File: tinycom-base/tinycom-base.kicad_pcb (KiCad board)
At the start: 2 copper layers, 45.2 x 45.2 mm, 38 parts, among them J1 MICRO_SD_HINGE, P1 CONN_02X08, P2 CONN_02X08, P3 USB_A, P4 USB_B, U1 SY8008BAAC, U2 SY8008BAAC, U3 SY8008BAAC

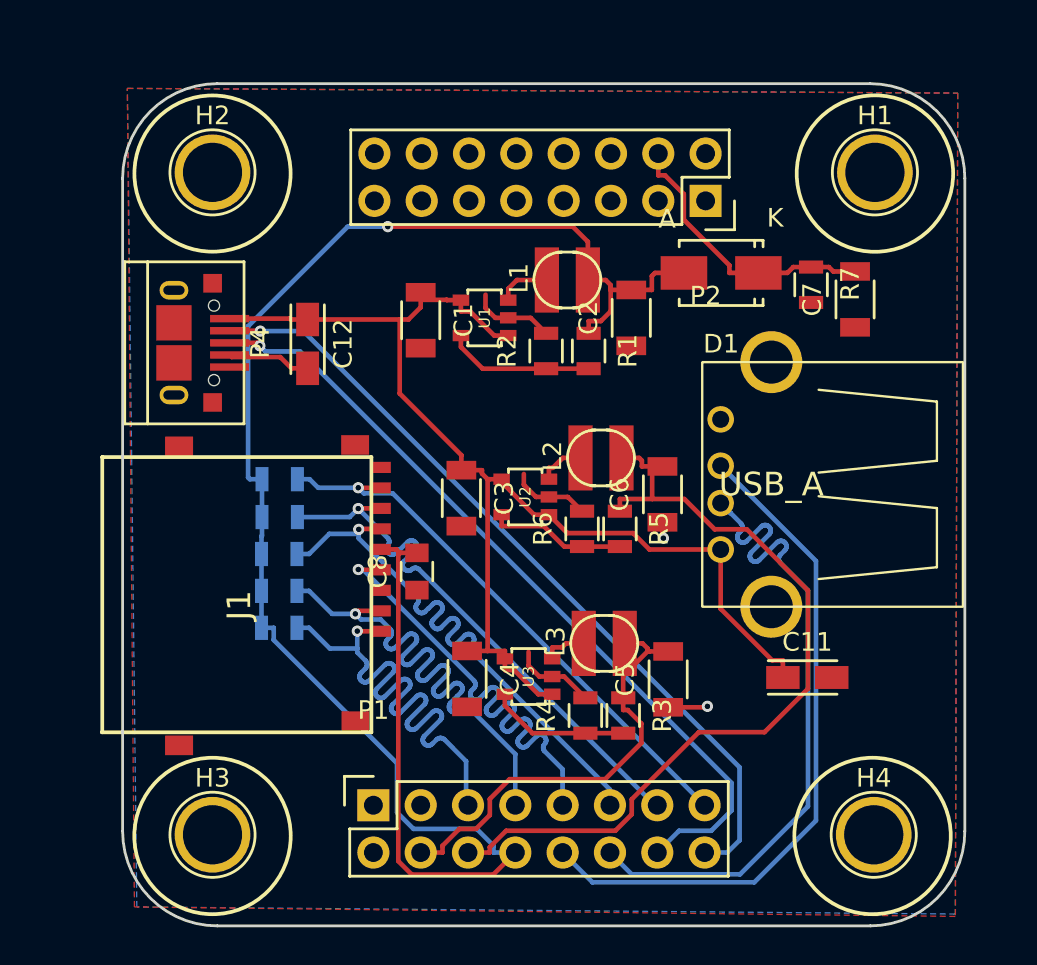
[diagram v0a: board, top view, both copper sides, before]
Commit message: add uboot_sel test point
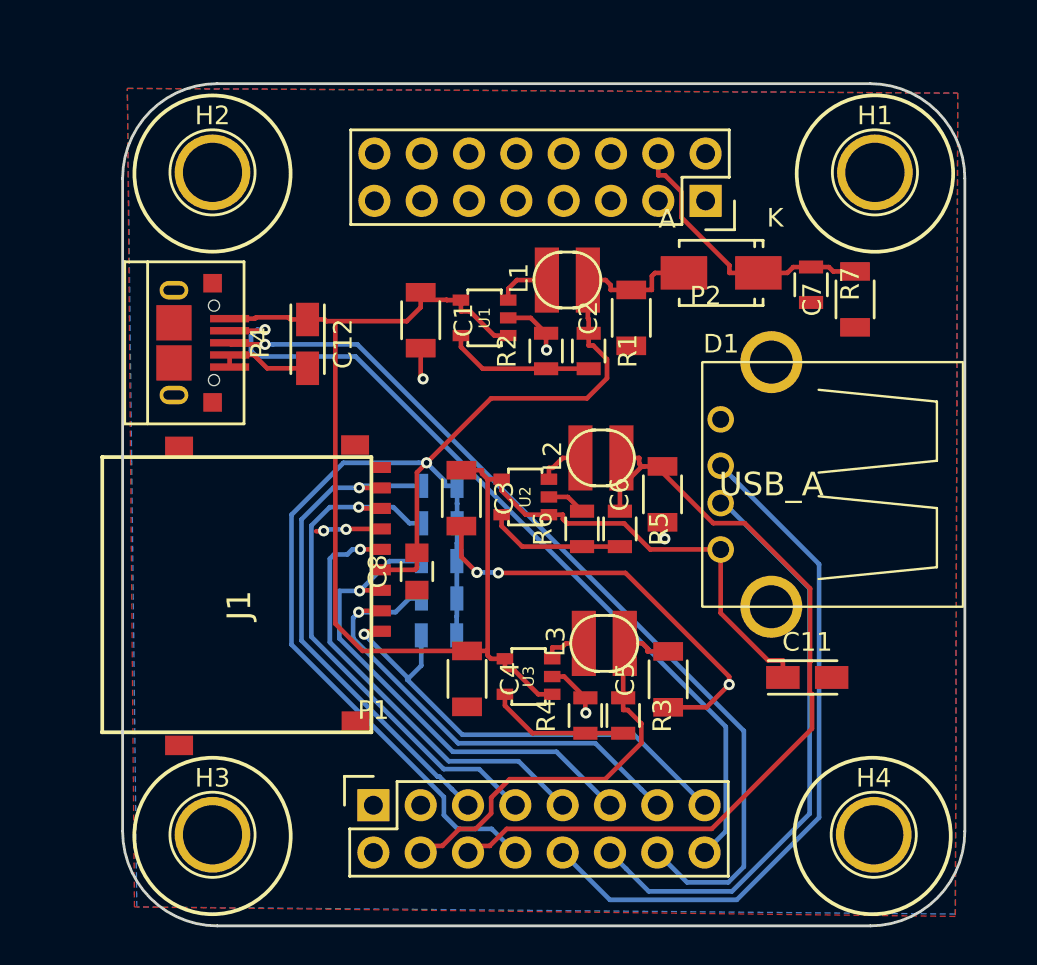
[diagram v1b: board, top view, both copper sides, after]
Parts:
- P4: value USB_B -> USB_OTG
- moved R12 12.0 mm to (141.4, 108.9), turned to 180 degrees
- moved R8 11.5 mm to (141.5, 100.8), turned to 180 degrees
- moved R11 9.61 mm to (141.5, 106.9), turned to 180 degrees
- moved R9 9.34 mm to (141.5, 102.8), turned to 180 degrees
- moved R10 8.59 mm to (141.5, 104.9), turned to 180 degrees
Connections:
- P4 pad 5: (no net) -> GND
- P4 pad 6: (no net) -> GND
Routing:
- net GND: track 20.8 -> 42.7 mm, vias 2 -> 9
- net VCC_33: track 95.8 -> 74.5 mm
- net +5V: track 66.6 -> 81.5 mm
- net UDP0: track 43.1 -> 49.2 mm
- net UDM1: track 37.6 -> 32.6 mm
- net SDC0_D2: track 30.3 -> 25.8 mm
- net SDC0_D3: track 30.3 -> 26.5 mm
- net SDC0_CMD: track 30.6 -> 27.0 mm
- net SDC0_CLK: track 26.7 -> 23.6 mm
- net SDC0_D1: track 30.5 -> 27.5 mm
- net SDC0_D0: track 30.5 -> 28.6 mm
- net UDM0: track 43.2 -> 44.7 mm
- net UDP1: track 36.8 -> 37.7 mm

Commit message: xxx
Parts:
- C12: footprint Capacitors_Tantalum_SMD:TantalC_SizeA_EIA-3216_Reflow -> Capacitors_Tantalum_SMD:TantalC_SizeB_EIA-3528_Reflow
- moved C12 0.12 mm to (134.3, 93.2)
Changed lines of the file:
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@@
     (links 90)
     (no_connects 0)
-    (area 124.384999 79.172999 169.747001 124.535001)
+    (area 122.516 73.697334 169.783501 124.987666)
     (thickness 1.6)
     (drawings 14)
@@
   )
   (module Capacitors_Tantalum_SMD:TantalC_SizeA_EIA-3216_Reflow (layer F.Cu)
-    (at 134.391 93.218 270)
-    (descr "Tantal Cap. , Size A, EIA-3216, Reflow")
-    (tags "Tantal Capacitor Size-A EIA-3216 reflow")
-    (attr smd)
-    (fp_text reference C12 (at 0 -1.9 270) (layer F.SilkS)
-      (effects (font (size 1 1) (thickness 0.15)))
-    )
-    (fp_text value CP_Small (at 0 2.1 270) (layer F.Fab)
-      (effects (font (size 1 1) (thickness 0.15)))
-    )
-    (fp_line (start 1.6 0.9) (end -2.1 0.9) (layer F.SilkS) (width 0.15))
-    (fp_line (start 1.6 -0.9) (end -2.1 -0.9) (layer F.SilkS) (width 0.15))
-    (fp_line (start -2.5 1.2) (end 2.5 1.2) (layer F.CrtYd) (width 0.05))
-    (fp_line (start 2.5 1.2) (end 2.5 -1.2) (layer F.CrtYd) (width 0.05))
-    (fp_line (start 2.5 -1.2) (end -2.5 -1.2) (layer F.CrtYd) (width 0.05))
-    (fp_line (start -2.5 -1.2) (end -2.5 1.2) (layer F.CrtYd) (width 0.05))
-    (pad 2 smd rect (at 1.31 0 270) (size 1.8 1.23) (layers F.Cu F.Paste F.Mask)
-      (net 2 GND))
-    (pad 1 smd rect (at -1.31 0 270) (size 1.8 1.23) (layers F.Cu F.Paste F.Mask)
-      (net 1 +5V))
-    (model Capacitors_Tantalum_SMD.3dshapes/TantalC_SizeA_EIA-3216_Reflow.wrl
-      (at (xyz 0 0 0))
-      (scale (xyz 1 1 1))
-      (rotate (xyz 0 0 180))
-    )
-  )
-  (module Capacitors_Tantalum_SMD:TantalC_SizeA_EIA-3216_Reflow (layer F.Cu)
     (at 161.214 111.125)
     (descr "Tantal Cap. , Size A, EIA-3216, Reflow")
@@
     (pad 6 smd rect (at 3.2 -0.9) (size 1 1) (layers F.Cu F.Paste F.Mask)
       (net 2 GND))
+  )
+  (module Capacitors_Tantalum_SMD:TantalC_SizeB_EIA-3528_Reflow (layer F.Cu)
+    (at 134.27202 93.19972 270)
+    (descr "Tantal Cap. , Size B, EIA-3528, Reflow")
+    (tags "Tantal Capacitor Size-B EIA-3528 Reflow")
+    (attr smd)
+    (fp_text reference C12 (at 0 -2.6 270) (layer F.SilkS)
+      (effects (font (size 1 1) (thickness 0.15)))
+    )
+    (fp_text value CP_Small (at 0 2.7 270) (layer F.Fab)
+      (effects (font (size 1 1) (thickness 0.15)))
+    )
+    (fp_line (start 2.7 -1.8) (end -2.7 -1.8) (layer F.CrtYd) (width 0.05))
+    (fp_line (start -2.7 -1.8) (end -2.7 1.8) (layer F.CrtYd) (width 0.05))
+    (fp_line (start -2.7 1.8) (end 2.7 1.8) (layer F.CrtYd) (width 0.05))
+    (fp_line (start 2.7 1.8) (end 2.7 -1.8) (layer F.CrtYd) (width 0.05))
+    (fp_line (start 1.8 1.5) (end -2.3 1.5) (layer F.SilkS) (width 0.15))
+    (fp_line (start 1.8 -1.5) (end -2.3 -1.5) (layer F.SilkS) (width 0.15))
+    (pad 2 smd rect (at 1.46 0 270) (size 1.8 2.23) (layers F.Cu F.Paste F.Mask)
+      (net 2 GND))
+    (pad 1 smd rect (at -1.46 0 270) (size 1.8 2.23) (layers F.Cu F.Paste F.Mask)
+      (net 1 +5V))
+    (model Capacitors_Tantalum_SMD.3dshapes/TantalC_SizeB_EIA-3528_Reflow.wrl
+      (at (xyz 0 0 0))
+      (scale (xyz 1 1 1))
+      (rotate (xyz 0 0 180))
+    )
   )
   (gr_text http://tinycom.org/ (at 146.939 104.648) (layer B.SilkS)
@@
   (segment (start 144.0551 100.4825) (end 144.0551 109.701) (width 0.25) (layer F.Cu) (net 1))
   (segment (start 144.805 100.4825) (end 144.805 101.0926) (width 0.25) (layer F.Cu) (net 1))
+  (via (at 153.5684 103.67949) (size 0.6) (drill 0.3) (layers F.Cu B.Cu) (net 2))
   (segment (start 130.20354 93.812) (end 130.20354 94.462) (width 0.25) (layer F.Cu) (net 2))
   (segment (start 135.2296 103.2764) (end 134.8486 103.2764) (width 0.25) (layer F.Cu) (net 2))
@@
   (segment (start 153.441 102.795) (end 153.441 103.55209) (width 0.25) (layer F.Cu) (net 2))
   (segment (start 153.441 103.55209) (end 153.5684 103.67949) (width 0.25) (layer F.Cu) (net 2))
-  (via (at 153.5684 103.67949) (size 0.6) (drill 0.3) (layers F.Cu B.Cu) (net 2))
   (segment (start 140.462 93.448) (end 140.462 94.9706) (width 0.25) (layer F.Cu) (net 2))
   (segment (start 140.462 94.9706) (end 140.589 95.0976) (width 0.25) (layer F.Cu) (net 2))

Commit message: rename wifi->basse
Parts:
- removed C8: C_Small, Capacitors_SMD:C_0805
- removed R10, R11, R12, R8, R9: R_Small, Resistors_SMD:R_0805
- added HDMI1: HDMI-SWM-19, tinycom:HDMI-SWM-19, F.Cu at (128.6, 107.3)
- added U4: RTL8723BS(ComboModule), tinycom:RL-SM02BD(RTL8723BS), F.Cu at (146.8, 108.1)
- J1: moved to B.Cu
- moved J1 44.2 mm to (168.4, 102.1)
- moved C12 36.4 mm to (165.9, 111.2), turned to 0 degrees
- moved C11 35.4 mm to (132.2, 90.8), turned to 90 degrees
- moved C5 22.1 mm to (153.6, 89.1), turned to 180 degrees
- moved R3 22.1 mm to (155.6, 91.5), turned to 0 degrees
- moved R4 20.6 mm to (155.6, 93.5), turned to 180 degrees
- moved C4 18.9 mm to (155.5, 97.1)
- moved L3 16.8 mm to (151.7, 92.5), turned to 180 degrees
- moved U3 15.6 mm to (152.1, 96.6), turned to 180 degrees
- moved C6 14.2 mm to (146.0, 89.2), turned to 180 degrees
- moved C2 13.9 mm to (138.1, 89.1), turned to 180 degrees
- moved L1 12.6 mm to (136.1, 92.5), turned to 180 degrees
- moved R5 12.1 mm to (147.9, 91.5), turned to 0 degrees
- moved R1 9.84 mm to (139.9, 91.4), turned to 0 degrees
- moved R6 9.70 mm to (147.9, 93.5), turned to 180 degrees
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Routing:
- net +5V: track 81.5 -> 0.00 mm
- net VCC_33: track 74.5 -> 0.00 mm, vias 1 -> 0
- net UDP0: track 49.2 -> 0.00 mm, vias 1 -> 0
- net VCC_14: track 45.3 -> 0.00 mm
- net UDM0: track 44.7 -> 0.00 mm, vias 1 -> 0
- net GND: track 42.7 -> 0.00 mm, vias 9 -> 0
- net UDP1: track 37.7 -> 0.00 mm
- net UDM1: track 32.6 -> 0.00 mm
- net SDC0_D0: track 28.6 -> 0.00 mm, vias 1 -> 0
- net SDC0_D1: track 27.5 -> 0.00 mm, vias 1 -> 0
- net SDC0_CMD: track 27.0 -> 0.00 mm, vias 1 -> 0
- net SDC0_D3: track 26.5 -> 0.00 mm, vias 1 -> 0
- net SDC0_D2: track 25.8 -> 0.00 mm, vias 1 -> 0
- net SDC0_CLK: track 23.6 -> 0.00 mm, vias 1 -> 0
- net VCC_15: track 23.4 -> 0.00 mm
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
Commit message: improve base board
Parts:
- added C8: C_Small, Capacitors_SMD:C_0805, B.Cu at (157.4, 99.8)
- added U5: rainsun-antenna, tinycom:rainsun-antenna, F.Cu at (158.8, 112.7)
- added U6: sata-smd, Connect:SATA-7_SMD, B.Cu at (170.9, 102.0)
- P1, P2: value CONN_02X08 -> CONN_02X10; footprint Socket_Strips:Socket_Strip_Straight_2x08 -> Socket_Strips:Socket_Strip_Straight_2x10
- U4: value RTL8723BS(ComboModule) -> RTL8188; footprint tinycom:RL-SM02BD(RTL8723BS) -> tinycom:RTL8188
- moved J1 42.7 mm to (125.8, 101.3), turned to 270 degrees
- moved P2 20.3 mm to (135.6, 82.9), turned to 0 degrees
- moved C12 11.8 mm to (155.1, 106.5), turned to 270 degrees
- moved P1 2.32 mm to (135.6, 118.2)
- moved P4 1.02 mm to (127.0, 92.7)
- moved U4 0.98 mm to (146.3, 109.0), turned to 180 degrees
- moved HDMI1 0.94 mm to (129.2, 108.1)
- moved C4 0.64 mm to (155.0, 96.7)
- moved C3 0.60 mm to (147.3, 96.8)
- moved C1 0.49 mm to (139.4, 97.0)
- moved C2 0.17 mm to (138.0, 89.0)
- moved C5 0.17 mm to (153.5, 89.0)
- moved L2 0.17 mm to (143.9, 92.4)
- moved L3 0.17 mm to (151.6, 92.4)
- moved R3 0.17 mm to (155.4, 91.4)
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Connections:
- HDMI1 pad 1: (no net) -> HTX2P
- HDMI1 pad 10: (no net) -> HTXCP
- HDMI1 pad 11: (no net) -> GND
- HDMI1 pad 12: (no net) -> HTXCN
- HDMI1 pad 13: (no net) -> HCEC
- HDMI1 pad 15: (no net) -> HCSL
- HDMI1 pad 16: (no net) -> HSDA
- HDMI1 pad 17: (no net) -> GND
- HDMI1 pad 18: (no net) -> +5V
- HDMI1 pad 19: (no net) -> HHPD
- HDMI1 pad 2: (no net) -> GND
- HDMI1 pad 3: (no net) -> HTX2N
- HDMI1 pad 4: (no net) -> HTX1P
- HDMI1 pad 5: (no net) -> GND
- HDMI1 pad 6: (no net) -> HTX1N
- HDMI1 pad 7: (no net) -> HTX0P
- HDMI1 pad 8: (no net) -> GND
- HDMI1 pad 9: (no net) -> HTX0N
- P1 pad 1: (no net) -> HTX2P
- P1 pad 11: SDC0_CMD -> HTX0N
- P1 pad 13: SDC0_D3 -> HTXCP
- P1 pad 14: UDP0 -> UDP2
- P1 pad 15: SDC0_D2 -> HTXCN
- P1 pad 16: UDM0 -> UDM2
- P1 pad 3: (no net) -> HTX2N
- P1 pad 4: VCC_15 -> GND
- P1 pad 5: SDC0_D1 -> HTX1P
- P1 pad 6: VCC_14 -> UDP0
- P1 pad 7: SDC0_D0 -> HTX1N
- P1 pad 8: VCC_33 -> UDM0
- P1 pad 9: SDC0_CLK -> HTX0P
- P2 pad 1: (no net) -> VCC_33
- P2 pad 10: (no net) -> SDC0_D2
- P2 pad 12: (no net) -> SDC0_D3
- P2 pad 14: (no net) -> SDC0_CMD
- P2 pad 16: (no net) -> SDC0_CLK
- P2 pad 2: GND -> (no net)
- P2 pad 3: (no net) -> VCC_30
- P2 pad 4: VCC_30 -> (no net)
- P2 pad 7: (no net) -> VCC_15
- P2 pad 9: (no net) -> VCC_14
- U4 pad 1: (no net) -> GND
- U4 pad 2: (no net) -> UDP2
- U4 pad 3: (no net) -> UDM2
- U4 pad 4: (no net) -> VCC_33
- U4 pad 5: (no net) -> GND
- U4 pad 6: (no net) -> Net-(U4-Pad6)
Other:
- net class Default: clearance 0.15 -> 0.2; trace_width 0.25 -> 0.2
- rule trace_clearance: 0.15 -> 0.2

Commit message: move sata
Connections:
- P2 pad 10: SDC0_D2 -> SDC0_D0
- P2 pad 12: SDC0_D3 -> SDC0_D1
- P2 pad 14: SDC0_CMD -> (no net)
- P2 pad 16: SDC0_CLK -> (no net)
- P2 pad 18: SDC0_D0 -> (no net)
- P2 pad 2: (no net) -> SDC0_D2
- P2 pad 20: SDC0_D1 -> (no net)
- P2 pad 4: (no net) -> SDC0_D3
- P2 pad 6: (no net) -> SDC0_CMD
- P2 pad 8: (no net) -> SDC0_CLK
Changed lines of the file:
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@@
   (general
     (links 106)
-    (no_connects 82)
+    (no_connects 83)
     (area 124.384999 79.172999 169.747001 124.535001)
     (thickness 1.6)
@@
     (pad 1 thru_hole rect (at 0 0) (size 1.7272 1.7272) (drill 1.016) (layers *.Cu *.Mask F.SilkS)
       (net 5 VCC_33))
-    (pad 2 thru_hole oval (at 0 2.54) (size 1.7272 1.7272) (drill 1.016) (layers *.Cu *.Mask F.SilkS))
+    (pad 2 thru_hole oval (at 0 2.54) (size 1.7272 1.7272) (drill 1.016) (layers *.Cu *.Mask F.SilkS)
+      (net 33 SDC0_D2))
     (pad 3 thru_hole oval (at 2.54 0) (size 1.7272 1.7272) (drill 1.016) (layers *.Cu *.Mask F.SilkS)
       (net 9 VCC_30))
-    (pad 4 thru_hole oval (at 2.54 2.54) (size 1.7272 1.7272) (drill 1.016) (layers *.Cu *.Mask F.SilkS))
+    (pad 4 thru_hole oval (at 2.54 2.54) (size 1.7272 1.7272) (drill 1.016) (layers *.Cu *.Mask F.SilkS)
+      (net 32 SDC0_D3))
     (pad 5 thru_hole oval (at 5.08 0) (size 1.7272 1.7272) (drill 1.016) (layers *.Cu *.Mask F.SilkS))
-    (pad 6 thru_hole oval (at 5.08 2.54) (size 1.7272 1.7272) (drill 1.016) (layers *.Cu *.Mask F.SilkS))
+    (pad 6 thru_hole oval (at 5.08 2.54) (size 1.7272 1.7272) (drill 1.016) (layers *.Cu *.Mask F.SilkS)
+      (net 31 SDC0_CMD))
     (pad 7 thru_hole oval (at 7.62 0) (size 1.7272 1.7272) (drill 1.016) (layers *.Cu *.Mask F.SilkS)
       (net 3 VCC_15))
-    (pad 8 thru_hole oval (at 7.62 2.54) (size 1.7272 1.7272) (drill 1.016) (layers *.Cu *.Mask F.SilkS))
+    (pad 8 thru_hole oval (at 7.62 2.54) (size 1.7272 1.7272) (drill 1.016) (layers *.Cu *.Mask F.SilkS)
+      (net 30 SDC0_CLK))
     (pad 9 thru_hole oval (at 10.16 0) (size 1.7272 1.7272) (drill 1.016) (layers *.Cu *.Mask F.SilkS)
       (net 4 VCC_14))
     (pad 10 thru_hole oval (at 10.16 2.54) (size 1.7272 1.7272) (drill 1.016) (layers *.Cu *.Mask F.SilkS)
-      (net 33 SDC0_D2))
+      (net 29 SDC0_D0))
     (pad 11 thru_hole oval (at 12.7 0) (size 1.7272 1.7272) (drill 1.016) (layers *.Cu *.Mask F.SilkS))
     (pad 12 thru_hole oval (at 12.7 2.54) (size 1.7272 1.7272) (drill 1.016) (layers *.Cu *.Mask F.SilkS)
-      (net 32 SDC0_D3))
+      (net 28 SDC0_D1))
     (pad 13 thru_hole oval (at 15.24 0) (size 1.7272 1.7272) (drill 1.016) (layers *.Cu *.Mask F.SilkS))
-    (pad 14 thru_hole oval (at 15.24 2.54) (size 1.7272 1.7272) (drill 1.016) (layers *.Cu *.Mask F.SilkS)
-      (net 31 SDC0_CMD))
+    (pad 14 thru_hole oval (at 15.24 2.54) (size 1.7272 1.7272) (drill 1.016) (layers *.Cu *.Mask F.SilkS))
     (pad 15 thru_hole oval (at 17.78 0) (size 1.7272 1.7272) (drill 1.016) (layers *.Cu *.Mask F.SilkS))
-    (pad 16 thru_hole oval (at 17.78 2.54) (size 1.7272 1.7272) (drill 1.016) (layers *.Cu *.Mask F.SilkS)
-      (net 30 SDC0_CLK))
+    (pad 16 thru_hole oval (at 17.78 2.54) (size 1.7272 1.7272) (drill 1.016) (layers *.Cu *.Mask F.SilkS))
     (pad 17 thru_hole oval (at 20.32 0) (size 1.7272 1.7272) (drill 1.016) (layers *.Cu *.Mask F.SilkS))
-    (pad 18 thru_hole oval (at 20.32 2.54) (size 1.7272 1.7272) (drill 1.016) (layers *.Cu *.Mask F.SilkS)
-      (net 29 SDC0_D0))
+    (pad 18 thru_hole oval (at 20.32 2.54) (size 1.7272 1.7272) (drill 1.016) (layers *.Cu *.Mask F.SilkS))
     (pad 19 thru_hole oval (at 22.86 0) (size 1.7272 1.7272) (drill 1.016) (layers *.Cu *.Mask F.SilkS)
       (net 2 GND))
-    (pad 20 thru_hole oval (at 22.86 2.54) (size 1.7272 1.7272) (drill 1.016) (layers *.Cu *.Mask F.SilkS)
-      (net 28 SDC0_D1))
+    (pad 20 thru_hole oval (at 22.86 2.54) (size 1.7272 1.7272) (drill 1.016) (layers *.Cu *.Mask F.SilkS))
     (model Socket_Strips.3dshapes/Socket_Strip_Straight_2x10.wrl
       (at (xyz 0.45 -0.05 0))
